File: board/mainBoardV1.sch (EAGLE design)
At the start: 11 parts, among them U1 STM32F051C8T

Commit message: initial board + LPC MCU
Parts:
- removed U$1: LIS3DSH, Sensors:LIS3DSH
- removed U$3: L3G4200D, Sensors:L3G4200D
- added HIGHG_ACCEL: LPS331AP, Sensors:LPS331AP
- added R2, R3: pullup, SparkFun-Passives:RESISTOR0603-RES
- added S1: (no value), SparkFun-Electromechanical:SWITCH-SPDT-SMD-A
- added X1: S4B-ZR, con-jst:S4B-ZR
- JP1: value (none) -> M4; device SparkFun-Connectors:M04JST -> Connector:M4
- renumbered U$4 to BARO
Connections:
- new net I2C1_SCL: BARO.SCL/SPC, HIGHG_ACCEL.SCL/SPC, R3.2, U1PB.PB10
- new net I2C1_SDA: BARO.SDA/SDI/SDO, HIGHG_ACCEL.SDA/SDI/SDO, R2.2, U1PB.PB11
- new net I2C2_SCL: U1PA.PF6
- new net I2C2_SDA: U1PA.PF7
- new net USART1_RX: U1PA.PA10
- new net USART1_TX: U1PA.PA9
- net 3.3V: now also BARO.VCCA, BARO.VDD_IO, HIGHG_ACCEL.VCCA, HIGHG_ACCEL.VDD, HIGHG_ACCEL.VDD_IO, R2.1, R3.1, U1PWR.VDD, U1PWR.VDDA; no longer U$1.VDD, U$3.VDD
- net GND: now also HIGHG_ACCEL.GND, U1CTL.BOOT0, U1CTL.NRST; no longer U$1.GND

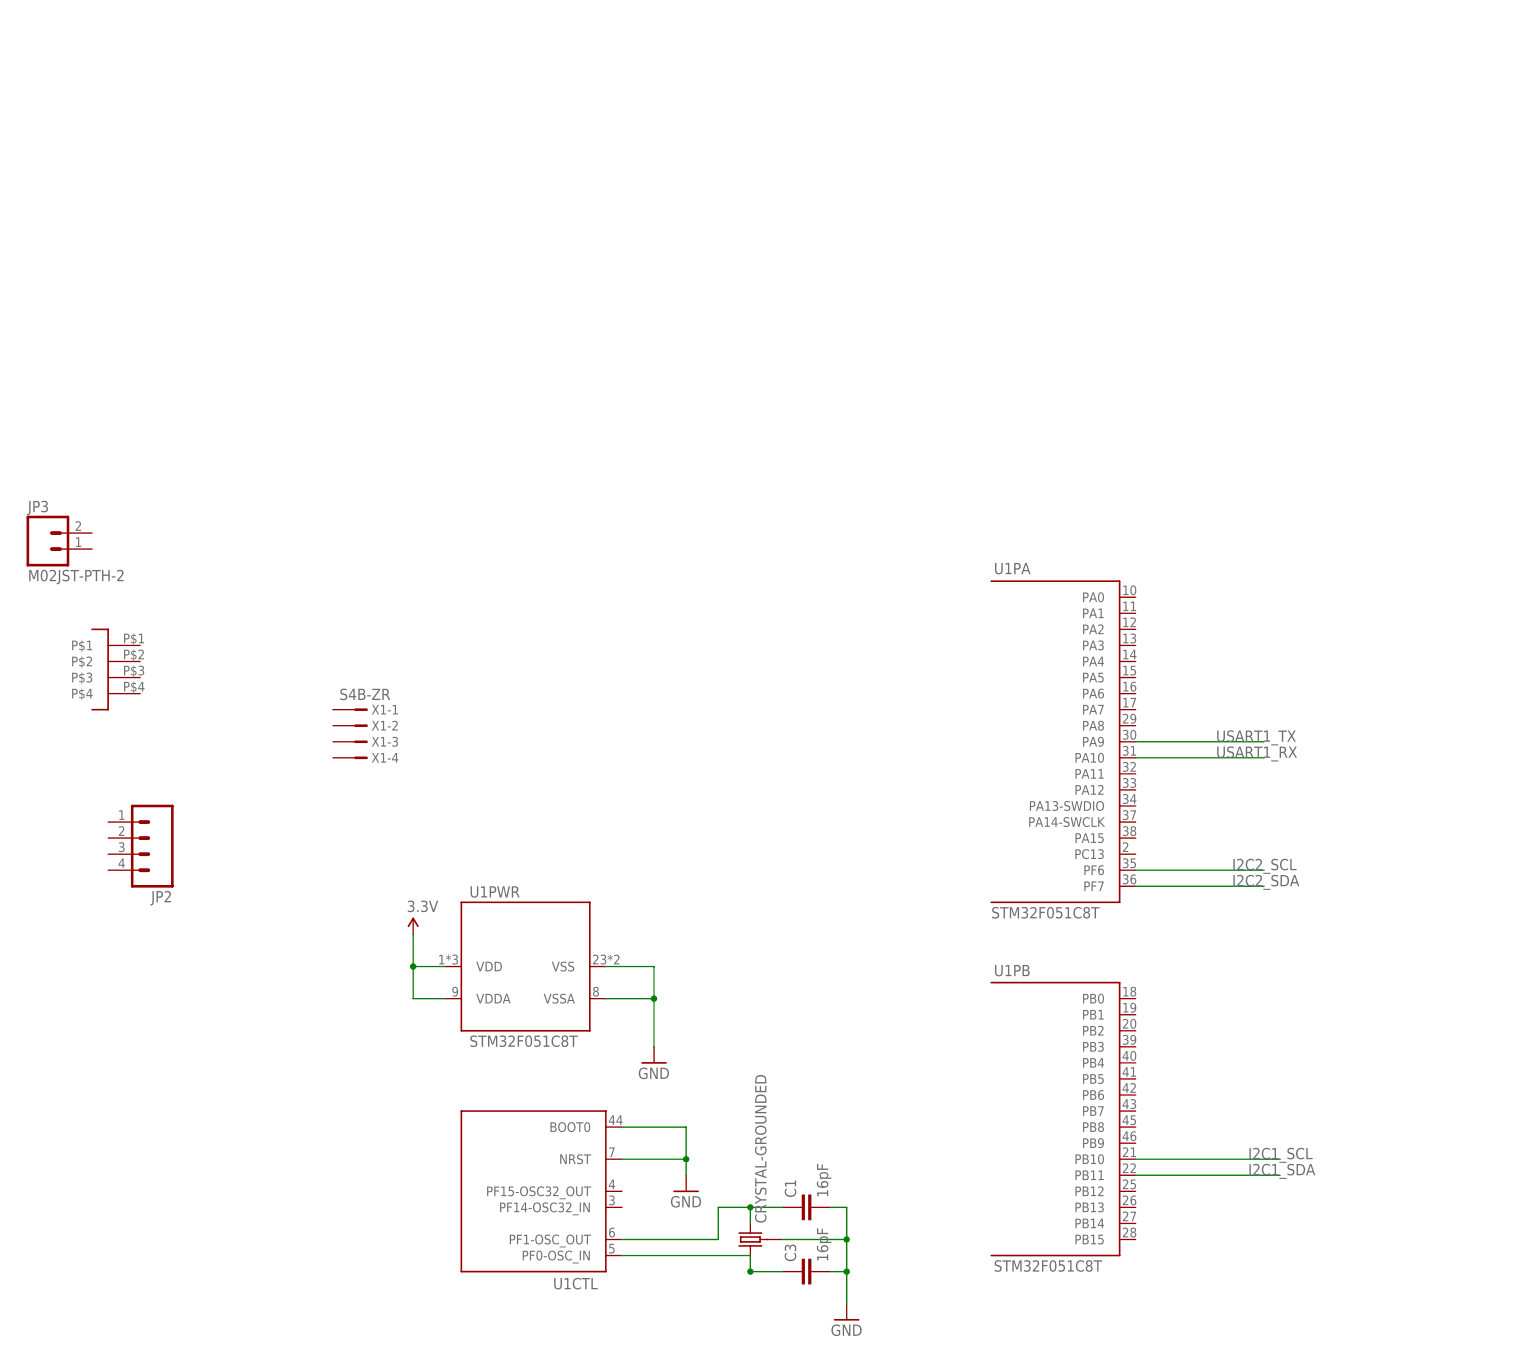
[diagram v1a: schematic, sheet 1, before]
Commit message: all major components on board, we have very little space
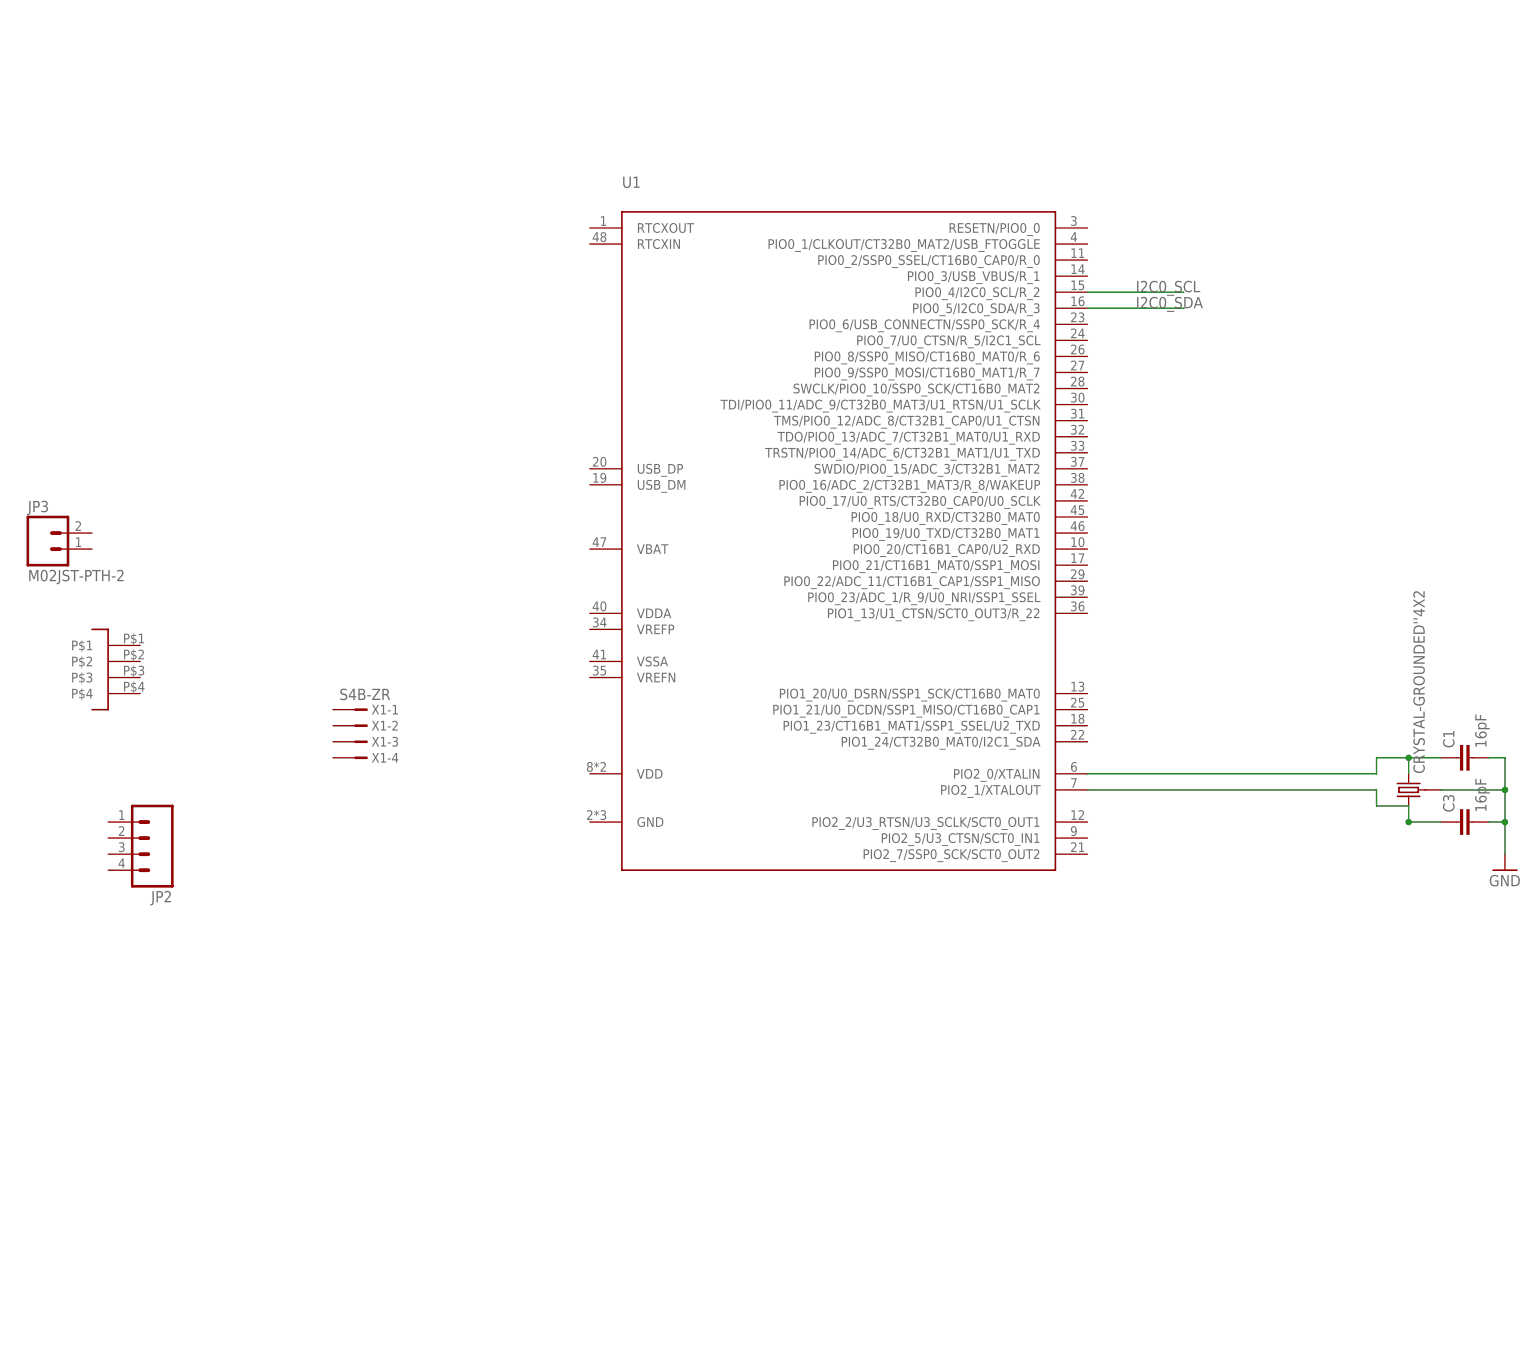
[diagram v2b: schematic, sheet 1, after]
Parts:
- added 9-AXIS: LSM9DS1, Sensors:LSM9DS1
- added U$1: ER-OLED0.84-1, Sensors:ER-OLED0.84-1
- added U$3: MICROSD-CD, Sensors:MICROSD-CD
- U$5: value CRYSTAL-GROUNDED -> CRYSTAL-GROUNDED''4X2; device SparkFun-FreqCtrl:CRYSTAL-GROUNDED -> SparkFun-FreqCtrl:CRYSTAL-GROUNDED''4X2
- U1: value STM32F051C8T -> (none); device STM32F030:STM32F051C8T -> LPC11U68:LPC11U68JBD48
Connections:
- removed net I2C1_SCL: BARO.SCL/SPC, HIGHG_ACCEL.SCL/SPC, R3.2, U1PB.PB10
- removed net I2C1_SDA: BARO.SDA/SDI/SDO, HIGHG_ACCEL.SDA/SDI/SDO, R2.2, U1PB.PB11
- removed net I2C2_SCL: U1PA.PF6
- removed net I2C2_SDA: U1PA.PF7
- removed net USART1_RX: U1PA.PA10
- removed net USART1_TX: U1PA.PA9
- new net I2C0_SCL: 9-AXIS.SCL/SPC, BARO.SCL/SPC, HIGHG_ACCEL.SCL/SPC, R3.2, U1.PIO0_4/I2C0_SCL/R_2
- new net I2C0_SDA: 9-AXIS.SDA/SDI/SDO, BARO.SDA/SDI/SDO, HIGHG_ACCEL.SDA/SDI/SDO, R2.2, U1.PIO0_5/I2C0_SDA/R_3
- net 3.3V: no longer U1PWR.VDD, U1PWR.VDDA
- net GND: no longer U1CTL.BOOT0, U1CTL.NRST, U1PWR.VSS, U1PWR.VSSA
- net N$2: now also U1.PIO2_1/XTALOUT; no longer U1CTL.PF0-OSC_IN
- net N$3: now also U1.PIO2_0/XTALIN; no longer U1CTL.PF1-OSC_OUT
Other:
- moved on the sheet: C1, C3

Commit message: board schematic ready for design review
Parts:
- removed JP2: (no value), SparkFun-Connectors:M04JST
- removed S1: (no value), SparkFun-Electromechanical:SWITCH-SPDT-SMD-A
- removed X1: S4B-ZR, con-jst:S4B-ZR
- added C10, C14, C15: 1uF, SparkFun-Passives:CAP0603-CAP
- added C11, C16, C17: 0.1uF, SparkFun-Passives:CAP0603-CAP
- added C12, C13, C9: 10uF, SparkFun-Passives:CAP0603-CAP
- added C2, C4: 1uF, SparkFun-Capacitors:CAP0603-CAP
- added C5, C6: 2.2uF, SparkFun-Capacitors:CAP0603-CAP
- added C7: 10nF, SparkFun-Capacitors:CAPPTH2
- added C8: 10uF, SparkFun-Capacitors:10UF-20V-10%(TANT)
- added JP4: USB_MICROB_PLUGCONN-11752, SparkFun-Connectors:USB_MICROB_PLUGCONN-11752
- added JP5, JP6: (no value), SparkFun-Connectors:M04JST
- added R1, R4: pullup, SparkFun-Passives:RESISTOR0402-RES
- added R5: (no value), SparkFun-Resistors:RESISTOR0603
- added R6, R7: 33, SparkFun-Passives:RESISTOR0603-RES
- added S2: DPDT, SparkFun-Electromechanical:SWITCH-DPDTAYZ0202
- added U$4: P82B715, Sensors:P82B715
- C1, C3: device SparkFun-Passives:CAP0603-CAP -> ELL-i-Passives:C0603
- JP1: value M4 -> M02JST-PTH-2; device Connector:M4 -> SparkFun-Connectors:M02JST-PTH-2
- JP3: value M02JST-PTH-2 -> M02-JST-2-PTH-NO_SILK; device SparkFun-Connectors:M02JST-PTH-2 -> SparkFun-Connectors:M02-JST-2-PTH-NO_SILK
- R2, R3: device SparkFun-Passives:RESISTOR0603-RES -> SparkFun-Passives:RESISTOR0402-RES
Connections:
- new net BARO_INT1: BARO.INT1, U1.TMS/PIO0_12/ADC_8/CT32B1_CAP0/U1_CTSN
- new net BARO_INT2: BARO.INT2, U1.TDO/PIO0_13/ADC_7/CT32B1_MAT0/U1_RXD
- new net HIGHG_INT1: HIGHG_ACCEL.INT1, U1.SWDIO/PIO0_15/ADC_3/CT32B1_MAT2
- new net HIGHG_INT2: HIGHG_ACCEL.INT2, U1.PIO0_16/ADC_2/CT32B1_MAT3/R_8/WAKEUP
- new net I2C1_SCL: JP1.1, R4.2, U$1.SCL, U$4.SY, U1.PIO0_7/U0_CTSN/R_5/I2C1_SCL
- new net I2C1_SDA: JP1.2, R1.2, U$1.SDA, U$4.SX, U1.PIO1_24/CT32B0_MAT0/I2C1_SDA
- new net I2CB2B_SCL: JP5.4, JP6.4, U$4.LY
- new net I2CB2B_SDA: JP5.3, JP6.3, U$4.LX
- new net INT1_A/G: 9-AXIS.INT1_A/G, U1.SWCLK/PIO0_10/SSP0_SCK/CT16B0_MAT2
- new net INT2_A/G: 9-AXIS.INT2_A/G, U1.TDI/PIO0_11/ADC_9/CT32B0_MAT3/U1_RTSN/U1_SCLK
- new net INT_M: 9-AXIS.INT_M, U1.TRSTN/PIO0_14/ADC_6/CT32B1_MAT1/U1_TXD
- new net N$1: JP3.1, S2.1
- new net N$10: C5.1, U$1.VCOMH
- new net N$11: 9-AXIS.CAP, C7.1
- new net N$12: R5.1, U$1.IREF
- new net N$13: C6.2, U$1.VBREF
- new net N$14: R6.2, U1.USB_DP
- new net N$15: JP4.D+, R6.1
- new net N$16: JP4.D-, R7.1
- new net N$17: R7.2, U1.USB_DM
- new net N$6: C4.1, U$1.C2P
- new net N$7: C4.2, U$1.C2N
- new net N$8: C2.1, U$1.C1P
- new net N$9: C2.2, U$1.C1N
- new net OLED_RST: U$1.RES_INV
- new net SSP1_MISO: U$3.DAT0, U1.PIO0_22/ADC_11/CT16B1_CAP1/SSP1_MISO
- new net SSP1_MOSI: U$3.CMD, U1.PIO0_21/CT16B1_MAT0/SSP1_MOSI
- new net SSP1_SCK: U$3.CLK, U1.PIO1_20/U0_DSRN/SSP1_SCK/CT16B0_MAT0
- new net SSP1_SSEL: U$3.CD/DAT3, U1.PIO0_23/ADC_1/R_9/U0_NRI/SSP1_SSEL
- new net USB_FTOGGLE: S2.5, U1.PIO0_1/CLKOUT/CT32B0_MAT2/USB_FTOGGLE
- new net USB_VBUS: JP4.VCC, S2.3
- new net VBUS: JP5.1, JP6.1, S2.2, U$2.EN, U$2.IN
- net 3.3V: now also 9-AXIS.CS_A/G, 9-AXIS.CS_M, 9-AXIS.DEN_A/G, 9-AXIS.SDO_AG, 9-AXIS.SDO_M, 9-AXIS.VDD, 9-AXIS.VDDIO, BARO.CS, BARO.SDO/SA0, C10.1, C11.1, C12.1, C13.1, C14.1, C15.1, C16.1, C17.1, C8.+, C9.1, HIGHG_ACCEL.CS, HIGHG_ACCEL.SDO/SA0, R1.1, R4.1, S2.6, U$1.VBAT, U$1.VCC, U$1.VDD, U$2.OUT, U$3.VDD, U$4.VCC, U1.PIO0_3/USB_VBUS/R_1, U1.RESETN/PIO0_0, U1.VBAT, U1.VDD, U1.VDDA, U1.VREFP
- net GND: now also 9-AXIS.GND, C10.2, C11.2, C12.2, C13.2, C14.2, C15.2, C16.2, C17.2, C5.2, C6.1, C7.2, C8.-, C9.2, JP3.2, JP4.GND, JP4.SHIELD, JP5.2, JP6.2, R5.2, S2.4, U$1.VSS, U$3.VSS, U$4.GND, U1.GND, U1.VREFN, U1.VSSA

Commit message: added a bunch of library files and docs
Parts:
- added C18: 10uF, ELL-i-Passives:CPOL1206
- added C19: 10uF, ELL-i-Passives:C0402
- added LED1, LED2: (no value), adafruit:LEDCHIPLED_0603
- added R8, R9: (no value), ELL-i-Passives:R0402
- added S1, S3: SWITCH-MOMENTARY-2-SMD-1101NE, SparkFun-Electromechanical:SWITCH-MOMENTARY-2-SMD-1101NE
- C1, C3: device ELL-i-Passives:C0603 -> ELL-i-Passives:C0402
- C10, C11, C12, C13, C14, C15, C16, C17, C9: device SparkFun-Passives:CAP0603-CAP -> ELL-i-Passives:C0402
- C2, C4, C5, C6: device SparkFun-Capacitors:CAP0603-CAP -> ELL-i-Passives:C0402
- C7: device SparkFun-Capacitors:CAPPTH2 -> ELL-i-Passives:C0402
- C8: device SparkFun-Capacitors:10UF-20V-10%(TANT) -> ELL-i-Passives:CPOL1206
- R1, R2, R3, R4: device SparkFun-Passives:RESISTOR0402-RES -> ELL-i-Passives:R0402
- R5: device SparkFun-Resistors:RESISTOR0603 -> ELL-i-Passives:R0402
- R6, R7: device SparkFun-Passives:RESISTOR0603-RES -> ELL-i-Passives:R0402
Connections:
- new net LED_PIN: LED2.A, U1.PIO0_17/U0_RTS/CT32B0_CAP0/U0_SCLK
- new net N$18: S3.1, U1.PIO0_9/SSP0_MOSI/CT16B0_MAT1/R_7
- new net N$19: S1.1, U1.PIO0_8/SSP0_MISO/CT16B0_MAT0/R_6
- new net N$4: LED1.C, R8.2
- new net N$5: LED2.C, R9.2
- net 3.3V: now also LED1.A, S1.2, S3.2
- net GND: now also C18.-, C19.2, R8.1, R9.1
- net VBUS: now also C18.+, C19.1
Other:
- moved on the sheet: C10, C11, C12, C13, C14, C15, C16, C17, C5, C7, C8, C9

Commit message: up to date board, some changes are still need in schemetic
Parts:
- U$5: value CRYSTAL-GROUNDED''4X2 -> CRYSTAL-GROUNDED2.5X2; device SparkFun-FreqCtrl:CRYSTAL-GROUNDED''4X2 -> SparkFun-FreqCtrl:CRYSTAL-GROUNDED2.5X2
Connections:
- removed net OLED_RST: U$1.RES_INV
- net 3.3V: now also U$1.RES_INV; no longer S1.2, S3.2
- net GND: now also S1.2, S3.2
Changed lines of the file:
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@@
 <part name="GND2" library="SparkFun-Aesthetics" deviceset="GND" device=""/>
 <part name="GND5" library="SparkFun-Aesthetics" deviceset="GND" device=""/>
-<part name="U$5" library="SparkFun-FreqCtrl" deviceset="CRYSTAL-GROUNDED" device="''4X2"/>
+<part name="U$5" library="SparkFun-FreqCtrl" deviceset="CRYSTAL-GROUNDED" device="2.5X2" value="CRYSTAL-GROUNDED2.5X2"/>
 <part name="C1" library="ELL-i-Passives" deviceset="C" device="0402" value="16pF"/>
 <part name="C3" library="ELL-i-Passives" deviceset="C" device="0402" value="16pF"/>
@@
 <part name="S1" library="SparkFun-Electromechanical" deviceset="SWITCH-MOMENTARY-2" device="-SMD-1101NE"/>
 <part name="S3" library="SparkFun-Electromechanical" deviceset="SWITCH-MOMENTARY-2" device="-SMD-1101NE"/>
-<part name="SUPPLY19" library="SparkFun-Aesthetics" deviceset="3.3V" device=""/>
+<part name="GND16" library="SparkFun-Aesthetics" deviceset="GND" device=""/>
 </parts>
 <sheets>
@@
 <instance part="S1" gate="G$1" x="142.24" y="152.4" rot="R90"/>
 <instance part="S3" gate="G$1" x="147.32" y="149.86" rot="R90"/>
-<instance part="SUPPLY19" gate="G$1" x="142.24" y="167.64"/>
+<instance part="GND16" gate="1" x="154.94" y="165.1"/>
 </instances>
 <busses>
@@
 <junction x="-58.42" y="160.02"/>
 </segment>
+<segment>
+<pinref part="S1" gate="G$1" pin="2"/>
+<wire x1="142.24" y1="157.48" x2="142.24" y2="167.64" width="0.1524" layer="91"/>
+<pinref part="S3" gate="G$1" pin="2"/>
+<wire x1="147.32" y1="167.64" x2="147.32" y2="154.94" width="0.1524" layer="91"/>
+<wire x1="142.24" y1="167.64" x2="147.32" y2="167.64" width="0.1524" layer="91"/>
+<pinref part="GND16" gate="1" pin="GND"/>
+<wire x1="147.32" y1="167.64" x2="154.94" y2="167.64" width="0.1524" layer="91"/>
+<junction x="147.32" y="167.64"/>
+</segment>
 </net>
 <net name="N$2" class="0">
 <segment>
-<pinref part="U$5" gate="G$1" pin="1"/>
-<pinref part="C3" gate="G$1" pin="1"/>
-<wire x1="157.48" y1="73.66" x2="165.1" y2="73.66" width="0.1524" layer="91"/>
-<wire x1="157.48" y1="73.66" x2="157.48" y2="76.2" width="0.1524" layer="91"/>
-<junction x="157.48" y="73.66"/>
-<wire x1="152.4" y1="76.2" x2="157.48" y2="76.2" width="0.1524" layer="91"/>
 <pinref part="U1" gate="G$1" pin="PIO2_1/XTALOUT"/>
 <wire x1="106.68" y1="78.74" x2="152.4" y2="78.74" width="0.1524" layer="91"/>
-<wire x1="152.4" y1="78.74" x2="152.4" y2="76.2" width="0.1524" layer="91"/>
+<wire x1="152.4" y1="78.74" x2="152.4" y2="73.66" width="0.1524" layer="91"/>
+<pinref part="C3" gate="G$1" pin="1"/>
+<wire x1="152.4" y1="73.66" x2="157.48" y2="73.66" width="0.1524" layer="91"/>
+<pinref part="U$5" gate="G$1" pin="1"/>
+<wire x1="157.48" y1="73.66" x2="165.1" y2="73.66" width="0.1524" layer="91"/>
+<wire x1="157.48" y1="76.2" x2="157.48" y2="73.66" width="0.1524" layer="91"/>
+<junction x="157.48" y="73.66"/>
 </segment>
 </net>
@@
 <wire x1="116.84" y1="160.02" x2="116.84" y2="167.64" width="0.1524" layer="91"/>
 <junction x="116.84" y="167.64"/>
-</segment>
-<segment>
-<pinref part="S1" gate="G$1" pin="2"/>
-<wire x1="142.24" y1="157.48" x2="142.24" y2="167.64" width="0.1524" layer="91"/>
-<pinref part="S3" gate="G$1" pin="2"/>
-<wire x1="142.24" y1="167.64" x2="147.32" y2="167.64" width="0.1524" layer="91"/>
-<wire x1="147.32" y1="167.64" x2="147.32" y2="154.94" width="0.1524" layer="91"/>
-<pinref part="SUPPLY19" gate="G$1" pin="3.3V"/>
-<junction x="142.24" y="167.64"/>
 </segment>
 </net>
@@
 <pinref part="U$1" gate="G$1" pin="VDD"/>
 <wire x1="68.58" y1="73.66" x2="76.2" y2="73.66" width="0.1524" layer="91"/>
-<wire x1="76.2" y1="73.66" x2="76.2" y2="88.9" width="0.1524" layer="91"/>
+<wire x1="76.2" y1="73.66" x2="76.2" y2="76.2" width="0.1524" layer="91"/>
 <junction x="76.2" y="88.9"/>
 <pinref part="SUPPLY8" gate="G$1" pin="3.3V"/>
+<pinref part="U$1" gate="G$1" pin="RES_INV"/>
+<wire x1="76.2" y1="76.2" x2="76.2" y2="88.9" width="0.1524" layer="91"/>
+<wire x1="68.58" y1="76.2" x2="76.2" y2="76.2" width="0.1524" layer="91"/>
+<junction x="76.2" y="76.2"/>
 </segment>
 <segment>
@@
 </segment>
 </net>
-<net name="OLED_RST" class="0">
-<segment>
-<pinref part="U$1" gate="G$1" pin="RES_INV"/>
-<wire x1="68.58" y1="76.2" x2="91.44" y2="76.2" width="0.1524" layer="91"/>
-<label x="83.82" y="76.2" size="1.778" layer="95"/>
-</segment>
-</net>
